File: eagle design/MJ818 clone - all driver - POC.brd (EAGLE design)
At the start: 35 x 35 mm, 37 parts, among them IC1 MAX16839, IC2 ATTINY4313-MMH, IC3 PRQV8.00CR1510Y00L, IC4 LDK320ADU50R, IC5 MCP2515, IC6 MCP2561-2, IC7 MAX16820, Q1 SiA456DJ, X1 CAN, X2 XPERED-L1-R250-00401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

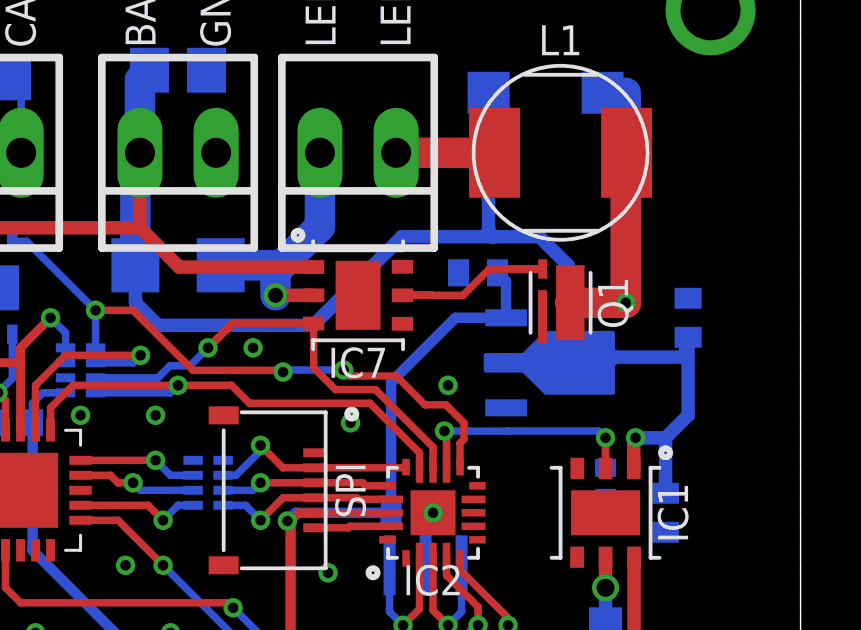
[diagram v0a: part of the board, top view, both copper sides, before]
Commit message: - recreated correctly named gerbers for mj818 POC
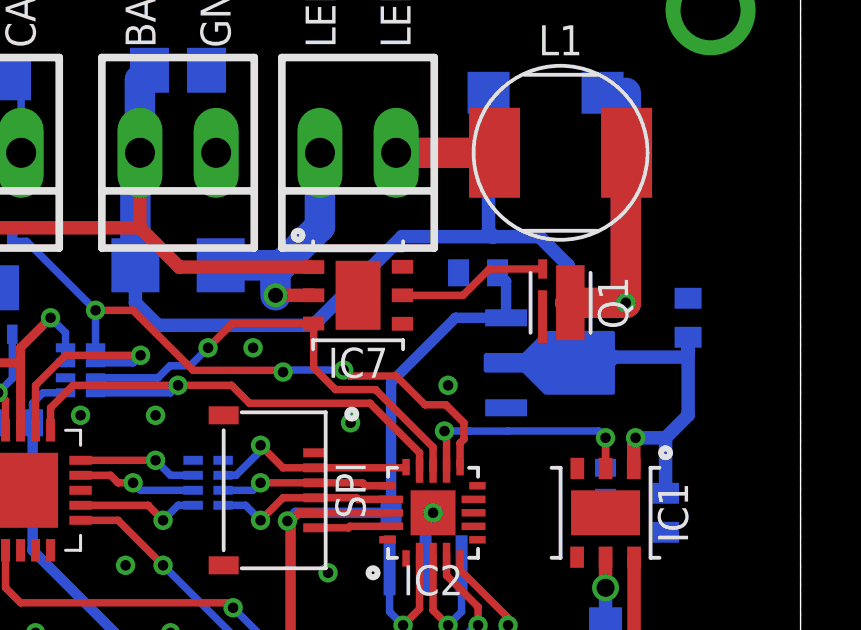
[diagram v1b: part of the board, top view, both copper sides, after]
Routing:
- net DIM_BRAKE_GATE: track 7.08 -> 5.04 mm
- net DIM_BRAKE: track 16.4 -> 15.4 mm
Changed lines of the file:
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@@
 <param name="mlMinCreamFrame" value="0mil"/>
 <param name="mlMaxCreamFrame" value="0mil"/>
-<param name="mlViaStopLimit" value="0.35mm"/>
+<param name="mlViaStopLimit" value="0.34mm"/>
 <param name="srRoundness" value="0"/>
 <param name="srMinRoundness" value="0mil"/>
@@
 <param name="dpGapFactor" value="2.5"/>
 <param name="checkAngle" value="1"/>
-<param name="checkFont" value="0"/>
+<param name="checkFont" value="1"/>
 <param name="checkRestrict" value="1"/>
 <param name="checkStop" value="0"/>
@@
 <wire x1="24.6" y1="24.604" x2="24.75" y2="24.454" width="0.508" layer="16"/>
 <wire x1="27.25" y1="20.4393375" x2="28.75" y2="20.4393375" width="0.508" layer="16"/>
-<wire x1="28.75" y1="20.4393375" x2="31.1606625" y2="20.4393375" width="0.45" layer="16"/>
-<wire x1="31.1606625" y1="20.4393375" x2="31.25" y2="21.1" width="0.508" layer="16"/>
+<wire x1="31.1606625" y1="20.4393375" x2="28.75" y2="20.4393375" width="0.45" layer="16"/>
 <wire x1="31.25" y1="18.5" x2="30.5" y2="17.75" width="0.45" layer="16"/>
 <wire x1="29.5" y1="17.75" x2="30.5" y2="17.75" width="0.45" layer="16"/>
@@
 <wire x1="13.578" y1="21.5" x2="18.75795" y2="21.5" width="0.45" layer="16"/>
 <wire x1="18.75795" y1="21.5" x2="21.71195" y2="24.454" width="0.45" layer="16"/>
+<wire x1="31.25" y1="21.1" x2="31.25" y2="20.528675" width="0.45" layer="16"/>
+<wire x1="31.25" y1="20.528675" x2="31.1606625" y2="20.4393375" width="0.45" layer="16"/>
 </signal>
 <signal name="GND">
@@
 <wire x1="13.58075625" y1="19.75" x2="13.98075625" y2="20.15" width="0.25" layer="16"/>
 <wire x1="13.98075625" y1="20.15" x2="14.65" y2="20.15" width="0.25" layer="16"/>
-<wire x1="15.25" y1="20.75" x2="16" y2="21.5" width="0.25" layer="1"/>
-<wire x1="18.77" y1="21.56" x2="16.06" y2="21.56" width="0.25" layer="1"/>
-<wire x1="16.06" y1="21.56" x2="15.25" y2="20.75" width="0.25" layer="1"/>
+<wire x1="16.06" y1="21.56" x2="18.77" y2="21.56" width="0.25" layer="1"/>
+<wire x1="15.25" y1="20.75" x2="16.06" y2="21.56" width="0.25" layer="1"/>
 </signal>
 <signal name="LED_AN" class="5">
@@
 <signal name="DIM_BRAKE_GATE" class="2">
 <contactref element="IC7" pad="DRV"/>
-<wire x1="22.75" y1="22.5" x2="21.73" y2="22.5" width="0.25" layer="1"/>
 <contactref element="Q1" pad="G"/>
-<wire x1="25.3761" y1="23.3761" x2="26.4034" y2="23.3761" width="0.25" layer="1"/>
-<wire x1="21.73" y1="22.5" x2="23.75" y2="22.5" width="0.25" layer="1"/>
 <wire x1="23.75" y1="22.5" x2="24.6261" y2="23.3761" width="0.25" layer="1"/>
 <wire x1="26.4034" y1="23.3761" x2="24.6261" y2="23.3761" width="0.25" layer="1"/>
+<wire x1="21.73" y1="22.5" x2="23.75" y2="22.5" width="0.25" layer="1"/>
 </signal>
 <signal name="LED_CA">

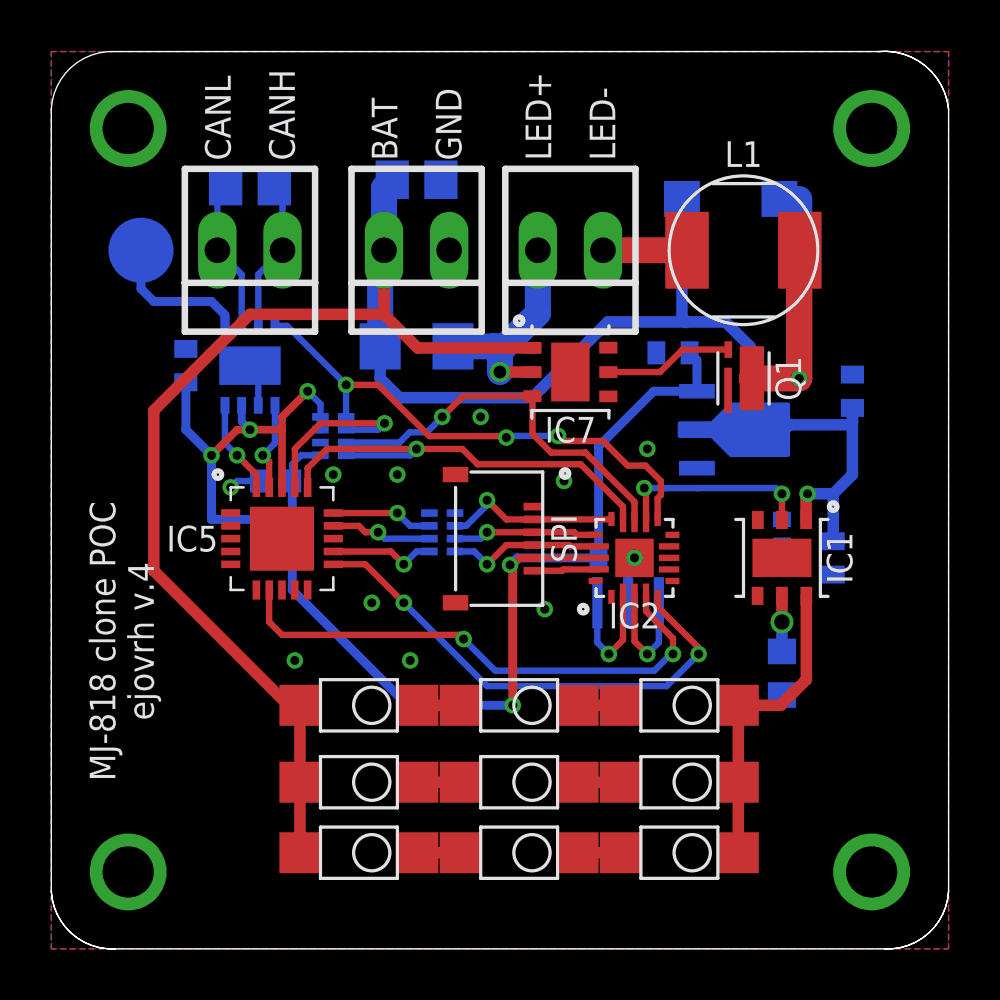
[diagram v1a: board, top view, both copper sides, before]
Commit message: - replaced oscillator, fet and mj808 utility led with better components, updated schematics - added/removed relevant datasheets for above changes
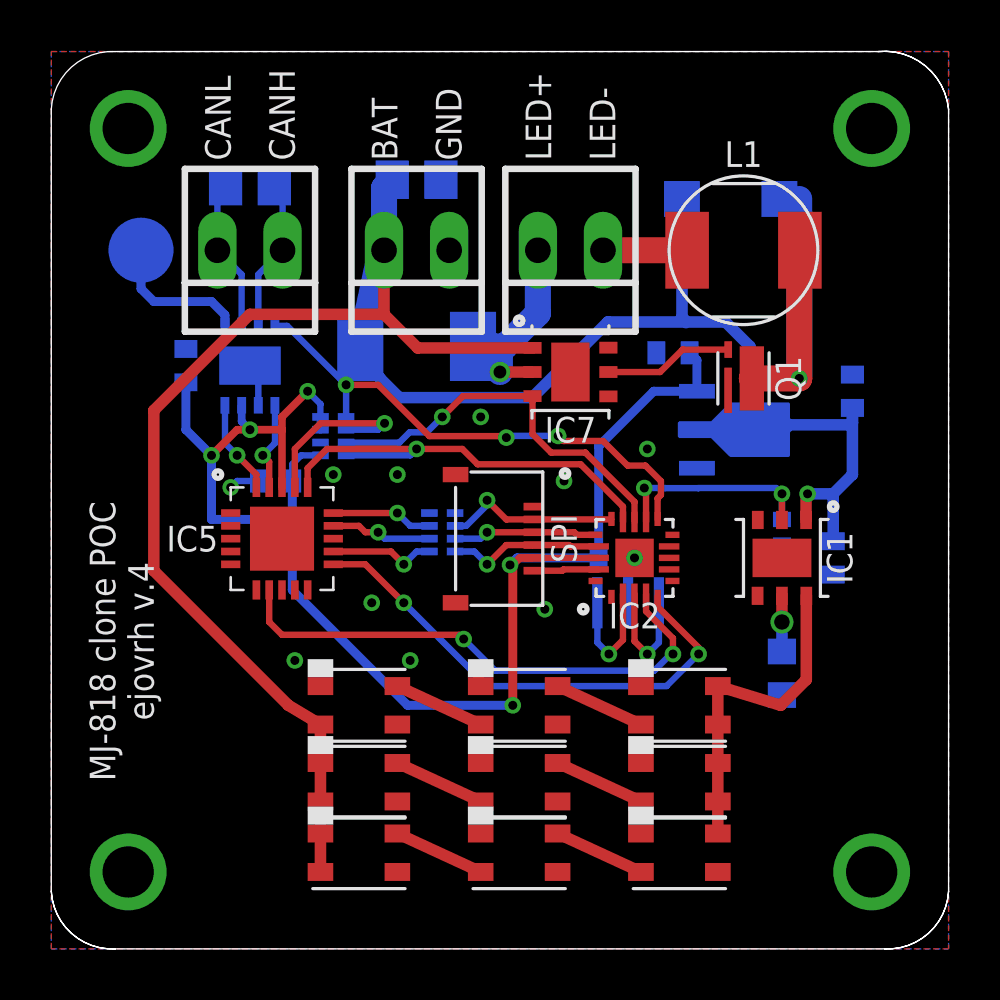
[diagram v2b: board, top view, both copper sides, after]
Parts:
- IC3: value PRQV8.00CR1510Y00L -> PBRC8.00GR50X000
- LED1, LED2, LED3, LED4, LED5, LED6, LED7, LED8, LED9: device AM2520SURC03-31454 - Red SMD LED:SMD -> 1374-CLM2D-RCC-ACC-1064252 - Red SMD LED:SMD
- Q1: value SiA456DJ -> SQA470EEJ-T1_GE3
- R6: value 30R/0.5W -> WSLT2010R2200FEB18 / 0.22Ohm 1W; device rcl:R1206 -> rcl:R2010
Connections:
- net 1.4: now also LED1.4, LED4.2; no longer LED1.C, LED4.A
- net 2.5: now also LED2.4, LED5.2; no longer LED2.C, LED5.A
- net 3.6: now also LED3.4, LED6.2; no longer LED3.C, LED6.A
- net 4.7: now also LED4.4, LED7.2; no longer LED4.C, LED7.A
- net 5.8: now also LED5.4, LED8.2; no longer LED5.C, LED8.A
- net 6.9: now also LED6.4, LED9.2; no longer LED6.C, LED9.A
- net BAT+: now also LED1.2, LED2.2, LED3.2; no longer LED1.A, LED2.A, LED3.A
- net SINK: now also LED7.4, LED8.4, LED9.4; no longer LED7.C, LED8.C, LED9.C
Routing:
- net 6.9: track 1.65 -> 3.58 mm
- net 5.8: track 1.65 -> 3.58 mm
- net 4.7: track 1.65 -> 3.58 mm
- net 3.6: track 1.65 -> 3.58 mm
- net 2.5: track 1.65 -> 3.58 mm
- net 1.4: track 1.65 -> 3.58 mm
- net BAT+: track 87.5 -> 88.8 mm
- net SINK: track 12.1 -> 13.0 mm
- net LED_AN: track 9.76 -> 8.98 mm
